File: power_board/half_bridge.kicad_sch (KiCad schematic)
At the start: 16 parts, among them Q1 IQD016N08NM5SCATMA1, Q2 IQD016N08NM5SCATMA1, U2 UCC27282DRCR

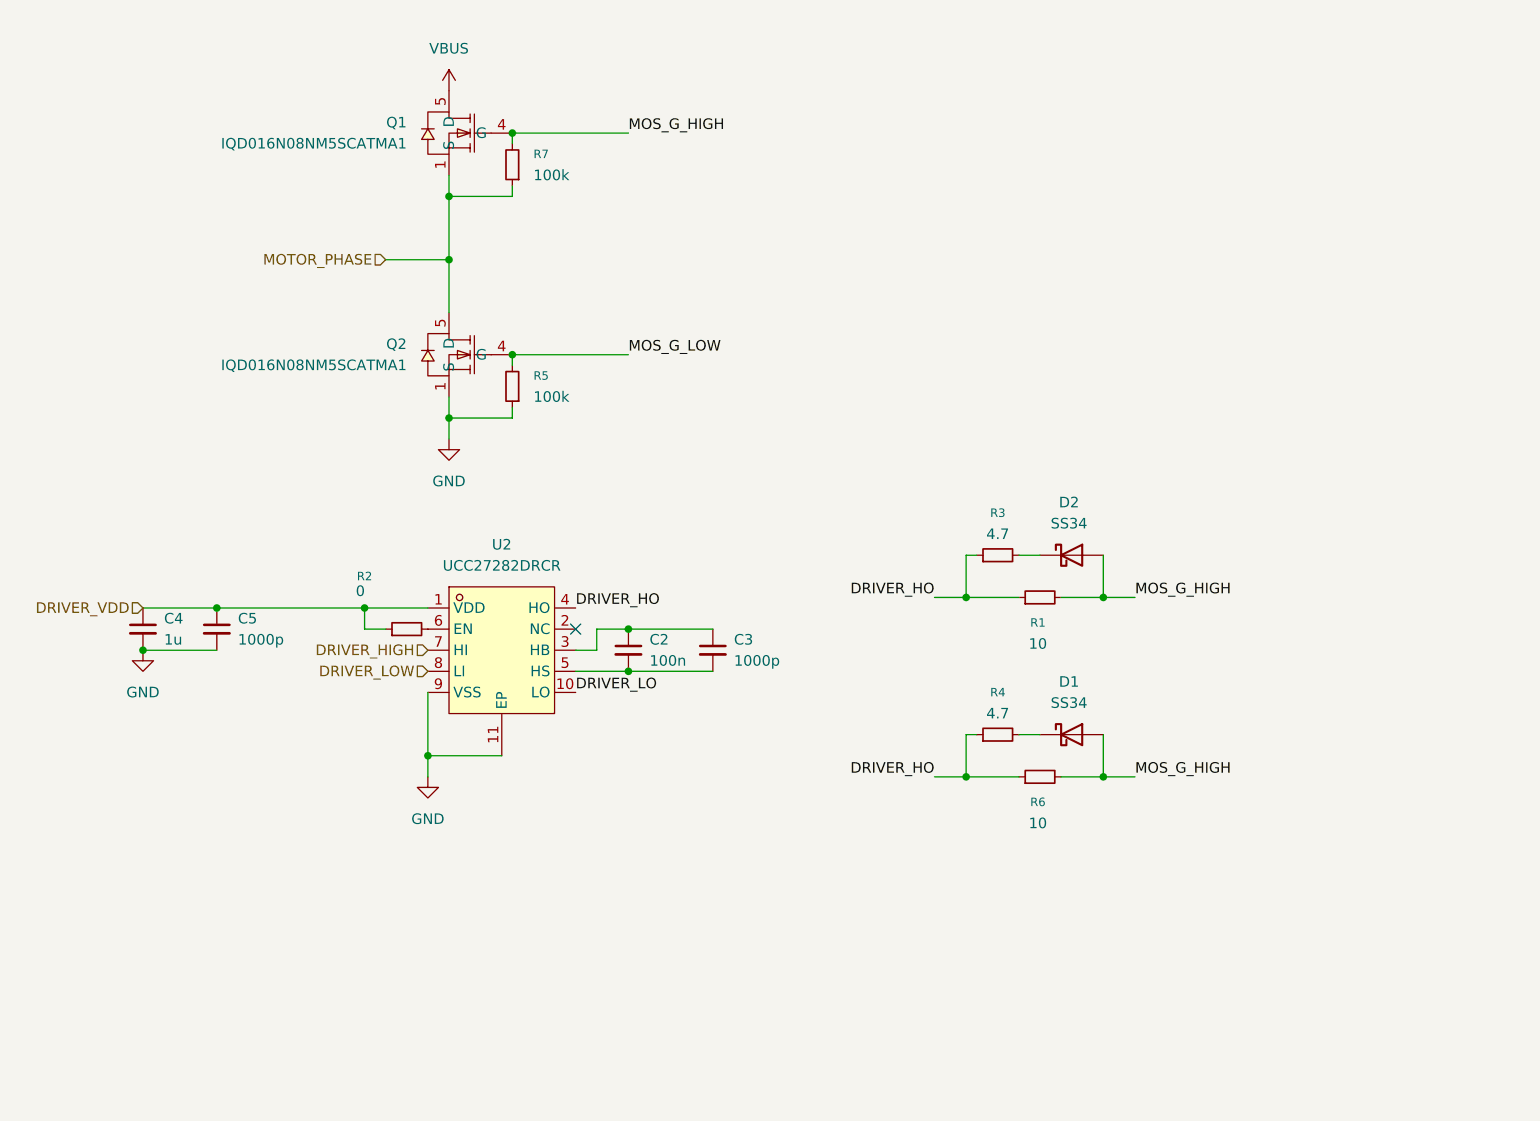
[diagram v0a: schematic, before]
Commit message: Seperat submodules into split sheets
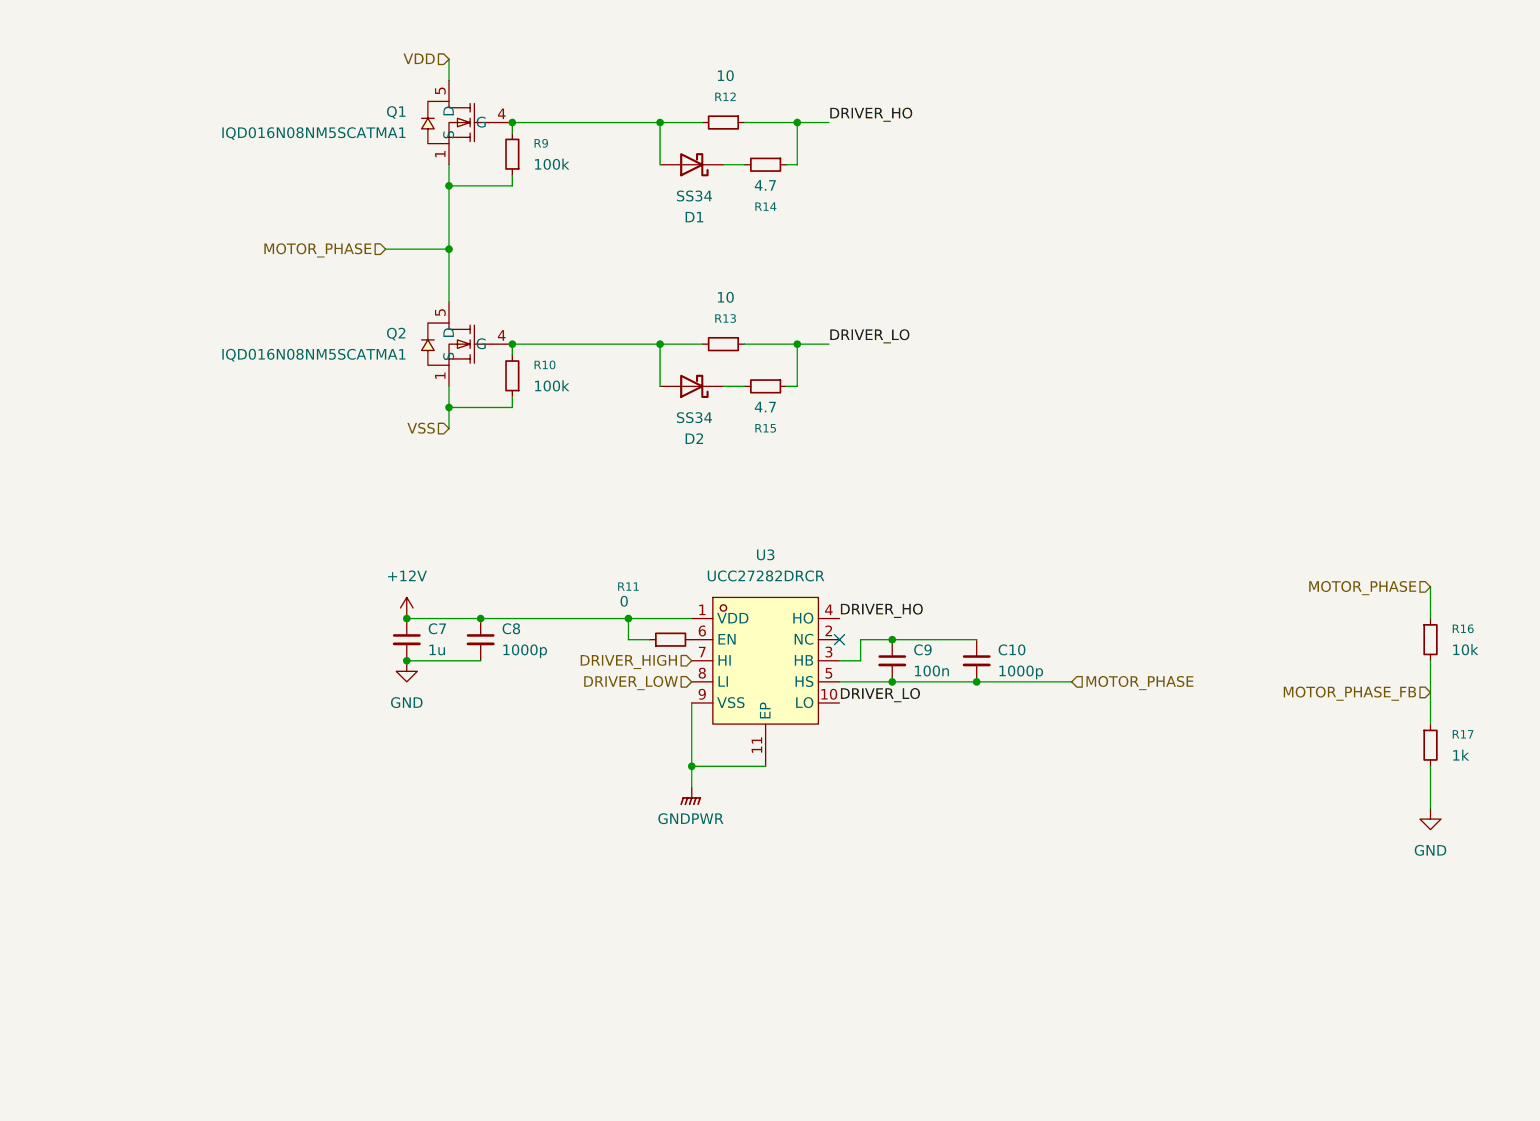
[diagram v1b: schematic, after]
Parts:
- added R16: 10k, symbol Device:R_Small
- added R17: 1k, symbol Device:R_Small
- renumbered C3 to C10, C4 to C7, C5 to C8, C2 to C9, D2 to D1, D1 to D2, R5 to R10, R2 to R11, R1 to R12, R6 to R13, R3 to R14, R4 to R15, R7 to R9, U2 to U3
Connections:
- net DRIVER_HO: no longer R13.1, R15.1
- net DRIVER_LO: now also R13.1, R15.1
- net GND: now also R17.2; no longer Q2.1 (S), R10.1, U3.11 (EP), U3.9 (VSS)
- net MOTOR_PHASE: now also C10.2, C9.2, U3.5 (HS), R16.1
- net DRIVER_VDD renamed +12V
- net MOS_G_HIGH: no longer names the net of D1.2 (A), Q1.4 (G), R12.2, R9.2
- net MOS_G_HIGH: no longer D2.2 (A), R13.2
- net MOS_G_LOW: no longer names the net of Q2.4 (G), R10.2
- net MOS_G_LOW: now also D2.2 (A), R13.2
- net VBUS renamed VDD
- new net GNDPWR: U3.11 (EP), U3.9 (VSS)
- new net MOTOR_PHASE_FB: R16.2, R17.1
- new net VSS: Q2.1 (S), R10.1
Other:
- moved on the sheet: C10, C7, C8, C9, D1, D2, Q1, Q2, R10, R11, R12, R13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

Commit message: Start multichannel layout
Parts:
- removed D1, D2: SS34, Diode_SMD:D_SMA, symbol Diode:SS34
- removed Q1, Q2: IQD016N08NM5SCATMA1, esc-library:PG-TSON-8_L6.0-W5.0_IQD020N10NM5ATMA1, symbol esc-library:IQD016N08NM5SCATMA1
- removed R11: 0, symbol Device:R_Small
- added D1, D2: B5819WS_C7420331, esc-library:SOD-323_L1.7-W1.3-LS2.5-FD, symbol esc-library:B5819WS_C7420331
- added Q1, Q2: BSC0702LS, esc-library:PG-TDSON-8_L5.0-W6.0-P1.27-BL-EP, symbol esc-library:BSC0702LS
- added U6: 66565S0M3, esc-library:CONN-SMD_66565S0M3, symbol esc-library:66565S0M3
- C13: renamed from C7; footprint (none) -> Capacitor_SMD:C_0603_1608Metric
- C14: renamed from C8; value 1000p -> 100n; footprint (none) -> Capacitor_SMD:C_0603_1608Metric
- C15: renamed from C9; footprint (none) -> Capacitor_SMD:C_0603_1608Metric
- C16: renamed from C10; footprint (none) -> Capacitor_SMD:C_0603_1608Metric
- R10: renamed from R15; footprint (none) -> Resistor_SMD:R_0603_1608Metric
- R11: renamed from R14; footprint (none) -> Resistor_SMD:R_0603_1608Metric
- R12: renamed from R13; footprint (none) -> Resistor_SMD:R_0603_1608Metric
- R13: renamed from R12; footprint (none) -> Resistor_SMD:R_0603_1608Metric
- R14: renamed from R10; footprint (none) -> Resistor_SMD:R_0603_1608Metric
- R15: renamed from R9; footprint (none) -> Resistor_SMD:R_0603_1608Metric
- R16, R17: footprint (none) -> Resistor_SMD:R_0603_1608Metric
- renumbered U3 to U5
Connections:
- net +12V: now also U5.6 (EN)
- net GND: no longer C13.2, C14.2
- net GNDPWR: now also C13.2, C14.2
- net MOTOR_PHASE: now also Q1.1 (S), Q1.2 (S), Q1.3 (S), Q2.5 (D), Q2.6 (D), Q2.7 (D), Q2.8 (D), U6.1
- net VDD: now also Q1.5 (D), Q1.6 (D), Q1.7 (D), Q1.8 (D)
- net VSS: now also Q2.1 (S), Q2.2 (S), Q2.3 (S)
- net at R13.2, R15.2: now also D2.1 (A), Q1.4 (G)
- net at R11.2: now also D2.2 (K)
- net at R12.2, R14.2: now also D1.1 (A), Q2.4 (G)
- net at R10.2: now also D1.2 (K)
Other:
- moved on the sheet: C13, C14, C15, C16, R10, R11, R12, R13, R14, R15, R16, R17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

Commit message: Complete primary layout step
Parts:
- added C13: 10u, Capacitor_SMD:C_1210_3225Metric, symbol Device:C_Small
- renumbered C14 to C10, C15 to C11, C16 to C12, C13 to C9, U5 to U3, U6 to U4
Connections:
- net VDD: now also C13.1
- net VSS: now also C13.2

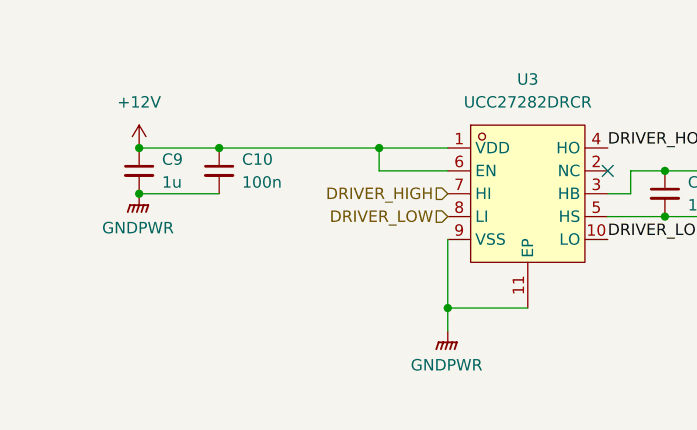
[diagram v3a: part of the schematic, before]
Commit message: Complete layout, and copper zone design
TODO!!!: move DCDC zone from GND area to PGND(current+)
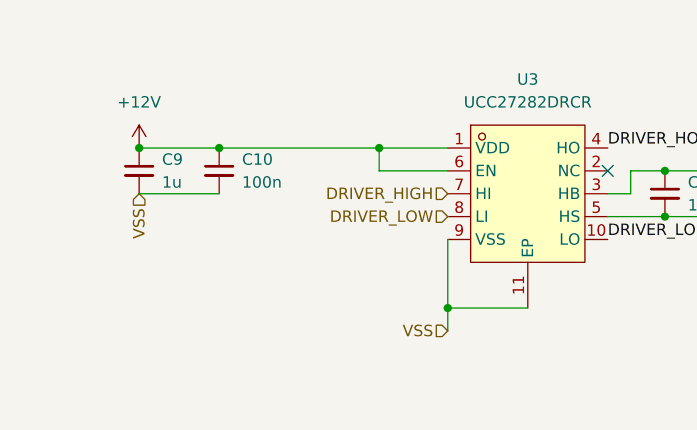
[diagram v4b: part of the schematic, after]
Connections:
- net GNDPWR is gone; now on net VSS: C10.2, C9.2, U3.11 (EP), U3.9 (VSS)
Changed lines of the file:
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@@
-	)
-	(junction
-		(at 60.96 134.62)
-		(diameter 0)
-		(color 0 0 0 0)
 	)
 	(junction
@@
 		)
 	)
+	(hierarchical_label "VSS"
+		(shape input)
+		(at 95.25 149.86 180)
+		(effects
+			(font
+				(size 1.27 1.27)
+			)
+			(justify right)
+		)
+	)
 	(hierarchical_label "MOTOR_PHASE"
 		(shape input)
@@
 		(shape input)
 		(at 95.25 137.16 180)
+		(effects
+			(font
+				(size 1.27 1.27)
+			)
+			(justify right)
+		)
+	)
+	(hierarchical_label "VSS"
+		(shape input)
+		(at 60.96 134.62 270)
 		(effects
 			(font
@@
 	)
 	(symbol
-		(lib_id "power:GNDPWR")
-		(at 95.25 149.86 0)
-		(unit 1)
-		(exclude_from_sim no)
-		(in_bom yes)
-		(on_board yes)
-		(dnp no)
-		(fields_autoplaced yes)
-		(property "Reference" "#PWR031"
-			(at 95.25 154.94 0)
-			(effects
-				(font
-					(size 1.27 1.27)
-				)
-				(hide yes)
-			)
-		)
-		(property "Value" "GNDPWR"
-			(at 95.123 153.67 0)
-			(effects
-				(font
-					(size 1.27 1.27)
-				)
-			)
-		)
-		(property "Footprint" ""
-			(at 95.25 151.13 0)
-			(effects
-				(font
-					(size 1.27 1.27)
-				)
-				(hide yes)
-			)
-		)
-		(property "Datasheet" ""
-			(at 95.25 151.13 0)
-			(effects
-				(font
-					(size 1.27 1.27)
-				)
-				(hide yes)
-			)
-		)
-		(property "Description" "Power symbol creates a global label with name \"GNDPWR\" , global ground"
-			(at 95.25 149.86 0)
-			(effects
-				(font
-					(size 1.27 1.27)
-				)
-				(hide yes)
-			)
-		)
-		(pin "1"
-		)
-		(instances
-			(project "power_board"
-				(path "/c786dd1f-c97f-4c1e-a27a-ac5828b3c50c/0fbb45d6-7cc5-4771-8820-af30fd089845"
-					(reference "#PWR036")
-					(unit 1)
-				)
-				(path "/c786dd1f-c97f-4c1e-a27a-ac5828b3c50c/38fb28ef-c920-476e-98e2-c5764b02e9b3"
-					(reference "#PWR031")
-					(unit 1)
-				)
-				(path "/c786dd1f-c97f-4c1e-a27a-ac5828b3c50c/74dd21af-da9a-49ef-aa54-e651b1250580"
-					(reference "#PWR041")
-					(unit 1)
-				)
-			)
-		)
-	)
-	(symbol
 		(lib_id "esc-library:UCC27282DRCR")
 		(at 104.14 134.62 0)
@@
 					(unit 1)
 				)
-			)
-		)
-	)
-	(symbol
-		(lib_id "power:GNDPWR")
-		(at 60.96 134.62 0)
-		(unit 1)
-		(exclude_from_sim no)
-		(in_bom yes)
-		(on_board yes)
-		(dnp no)
-		(fields_autoplaced yes)
-		(property "Reference" "#PWR030"
-			(at 60.96 139.7 0)
-			(effects
-				(font
-					(size 1.27 1.27)
-				)
-				(hide yes)
-			)
-		)
-		(property "Value" "GNDPWR"
-			(at 60.833 138.43 0)
-			(effects
-				(font
-					(size 1.27 1.27)
-				)
-			)
-		)
-		(property "Footprint" ""
-			(at 60.96 135.89 0)
-			(effects
-				(font
-					(size 1.27 1.27)
-				)
-				(hide yes)
-			)
-		)
-		(property "Datasheet" ""
-			(at 60.96 135.89 0)
-			(effects
-				(font
-					(size 1.27 1.27)
-				)
-				(hide yes)
-			)
-		)
-		(property "Description" "Power symbol creates a global label with name \"GNDPWR\" , global ground"
-			(at 60.96 134.62 0)
-			(effects
-				(font
-					(size 1.27 1.27)
-				)
-				(hide yes)
-			)
-		)
-		(pin "1"
-		)
-		(instances
-			(project "power_board"
-				(path "/c786dd1f-c97f-4c1e-a27a-ac5828b3c50c/0fbb45d6-7cc5-4771-8820-af30fd089845"
-					(reference "#PWR035")
-					(unit 1)
-				)
-				(path "/c786dd1f-c97f-4c1e-a27a-ac5828b3c50c/38fb28ef-c920-476e-98e2-c5764b02e9b3"
-					(reference "#PWR030")
-					(unit 1)
-				)
-				(path "/c786dd1f-c97f-4c1e-a27a-ac5828b3c50c/74dd21af-da9a-49ef-aa54-e651b1250580"
-					(reference "#PWR040")
-					(unit 1)
-				)

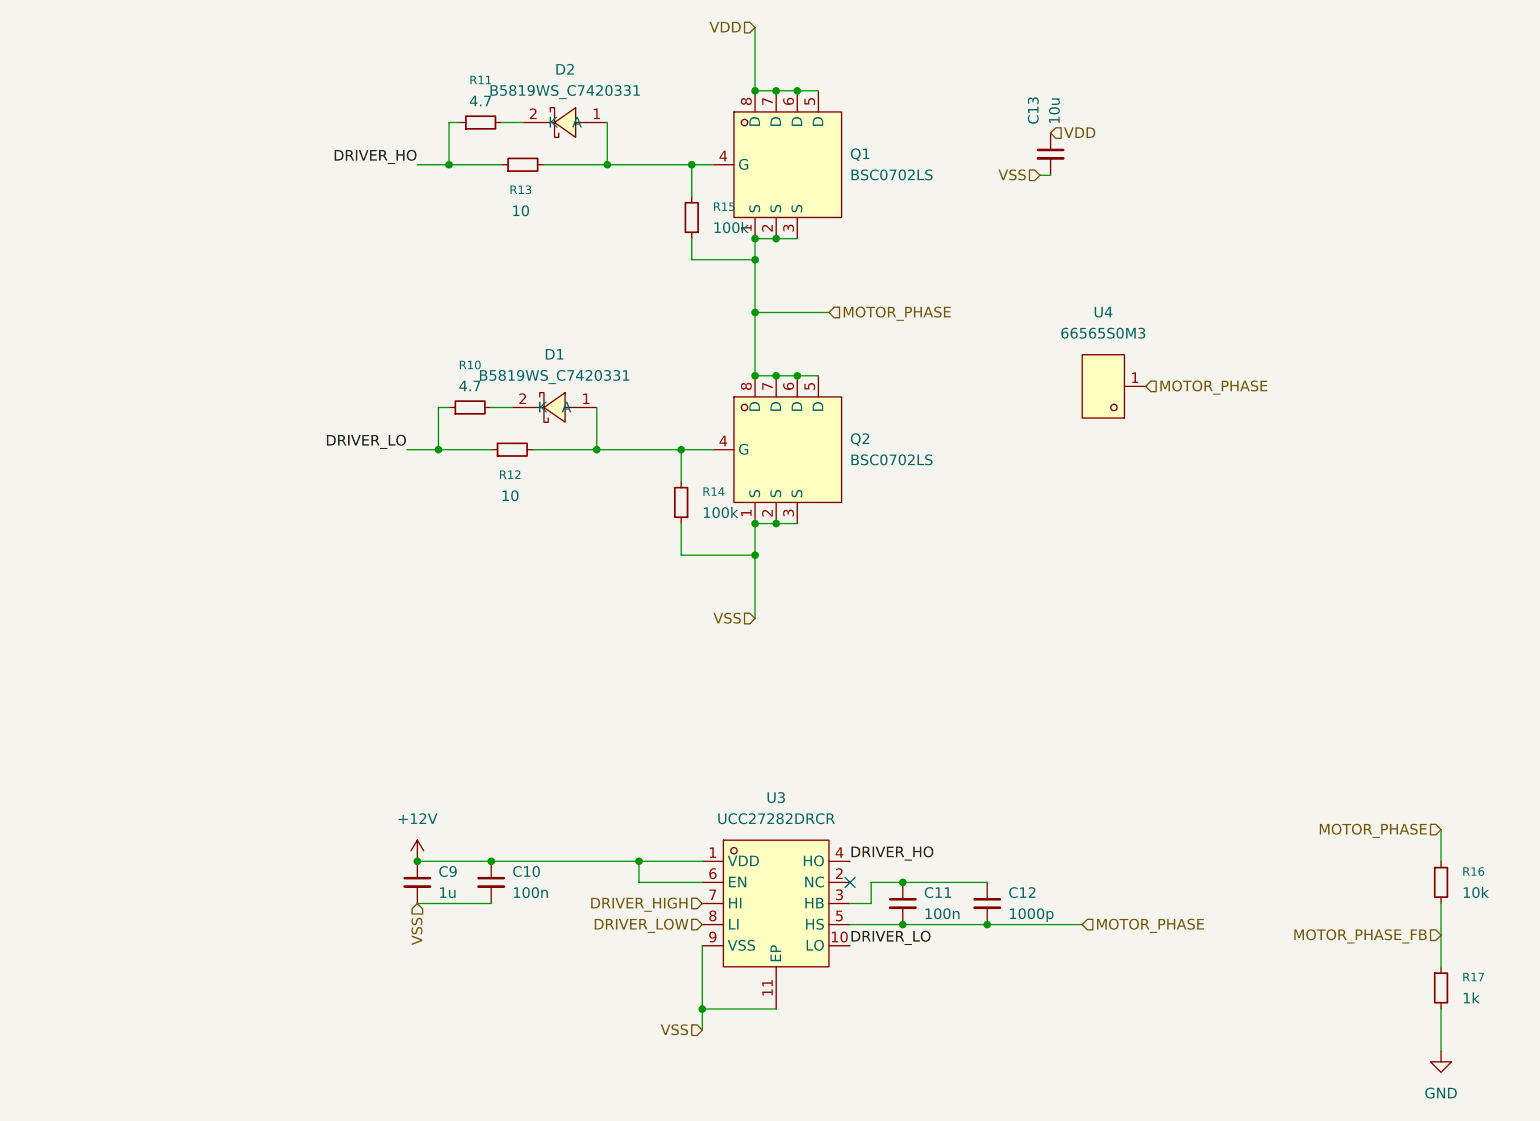
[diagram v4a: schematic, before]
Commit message: Add testpoint, SWD, and PWM port
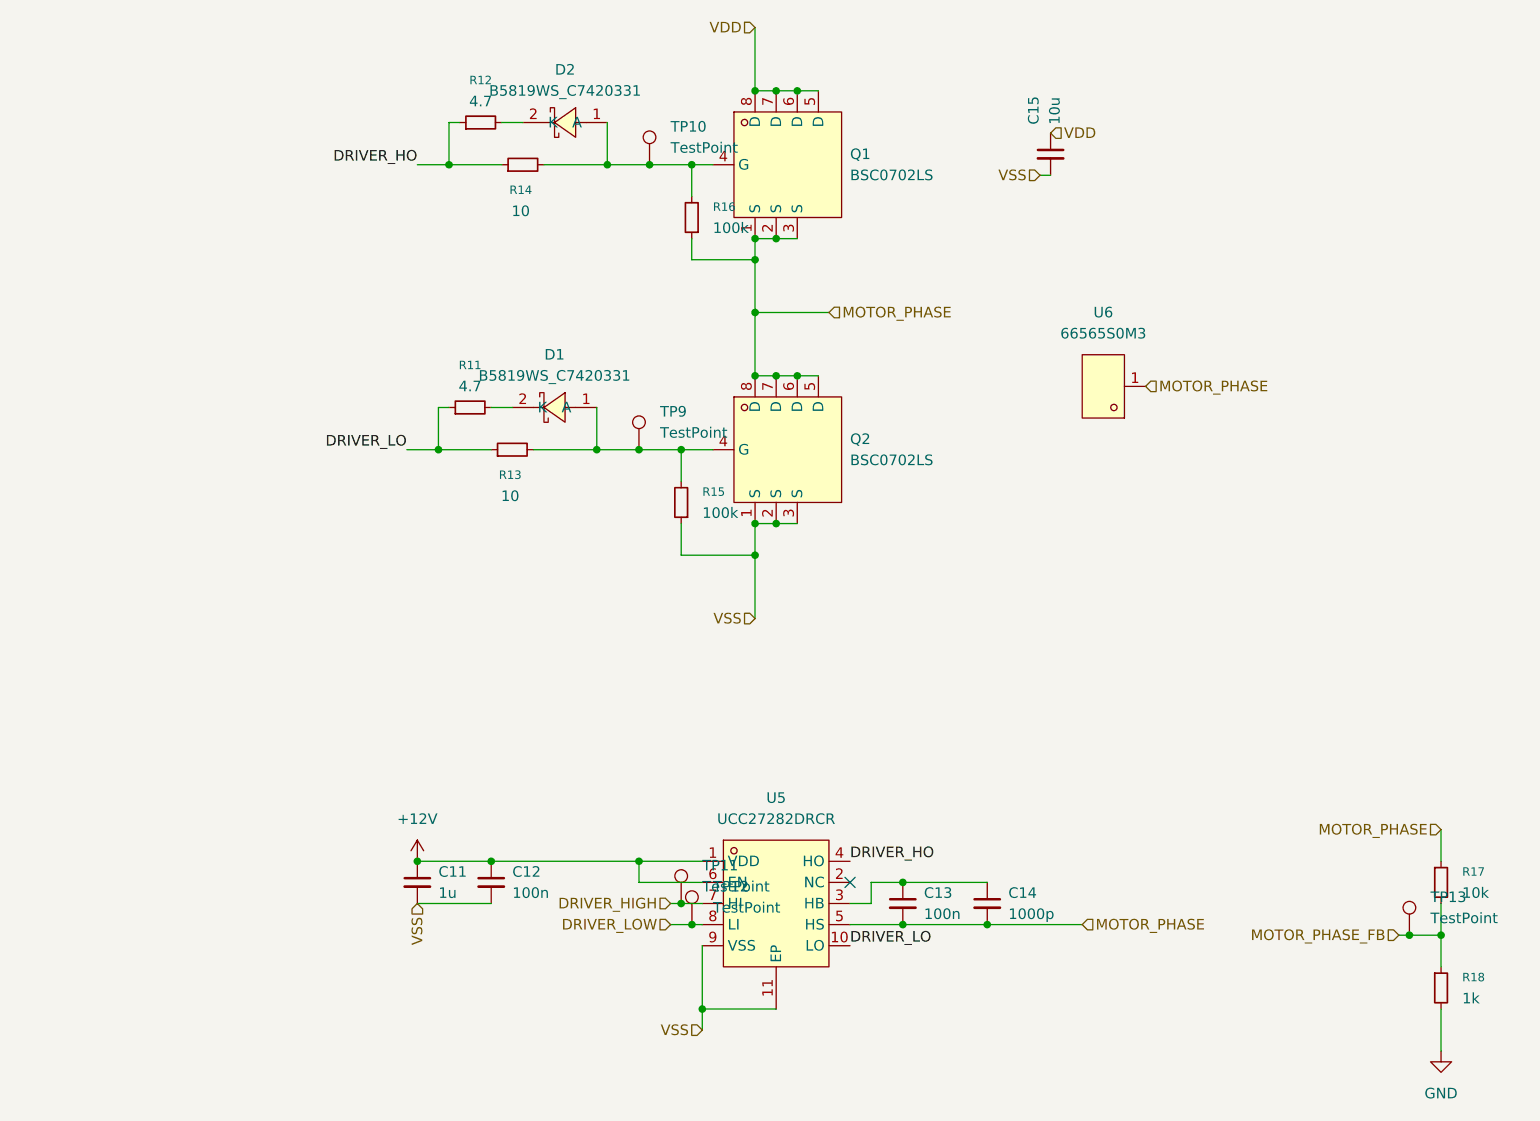
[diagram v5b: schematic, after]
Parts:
- added TP10, TP11, TP12, TP13, TP9: TestPoint, esc-library:SMD_RH-5015, symbol Connector:TestPoint
- renumbered C9 to C11, C10 to C12, C11 to C13, C12 to C14, C13 to C15, R10 to R11, R11 to R12, R12 to R13, R13 to R14, R14 to R15, R15 to R16, R16 to R17, R17 to R18, U3 to U5, U4 to U6
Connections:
- net DRIVER_HIGH: now also TP11.1
- net DRIVER_LOW: now also TP12.1
- net MOTOR_PHASE_FB: now also TP13.1
- net at D2.1 (A), Q1.4 (G), R14.2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: now also TP10.1
- net at D1.1 (A), Q2.4 (G), R13.2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: now also TP9.1
